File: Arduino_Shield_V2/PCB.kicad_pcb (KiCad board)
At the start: 2 copper layers, 68.6 x 53.3 mm, 18 parts, among them IC1 LTC6090HFE#PBF, J1 Power, J2 Digital/PWM, J3 Analog, J4 Digital/PWM, J6 Conn_01x01_Socket, U1 MCP4921

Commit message: Serious edits during 2/22 meeting by Eric
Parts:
- removed IC1: LTC6090HFE#PBF, LTC6090:SOP65P640X110-17N
- added C3: 0.1uF, Capacitor_SMD:C_1206_3216Metric_Pad1.33x1.80mm_HandSolder, F.Cu at (146.2, 81.5)
- added C4: 0.1uF, Capacitor_SMD:C_1206_3216Metric_Pad1.33x1.80mm_HandSolder, F.Cu at (131.5, 84.0)
- added J5: Conn_01x01, Connector_Pin:Pin_D1.0mm_L10.0mm, F.Cu at (160.4, 79.2)
- added J7: Conn_01x01, Connector_Pin:Pin_D1.0mm_L10.0mm, F.Cu at (160.4, 83.2)
- added J8: Conn_01x01, Connector_Pin:Pin_D1.0mm_L10.0mm, F.Cu at (160.4, 87.3)
- added U2: LTC6090, Package_SO:SOIC-8-1EP_3.9x4.9mm_P1.27mm_EP2.29x3mm, F.Cu at (138.3, 83.8)
- R1, R2, R3, R4, R5: footprint Resistor_THT:R_Axial_DIN0309_L9.0mm_D3.2mm_P12.70mm_Horizontal -> Resistor_SMD:R_1206_3216Metric_Pad1.30x1.75mm_HandSolder
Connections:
- J2 pad 1: /SCL/A5 -> unconnected-(J2-Pin_1-Pad1)
- J2 pad 2: /SDA/A4 -> unconnected-(J2-Pin_2-Pad2)
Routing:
- net GND: track 144.5 -> 0.00 mm, vias 3 -> 0
- net /SCL/A5: track 70.2 -> 0.00 mm
- net /SDA/A4: track 65.0 -> 0.00 mm
- net Net-(C2-Pad1): track 62.9 -> 16.0 mm
- net Net-(C2-Pad2): track 35.7 -> 14.3 mm
- net /*6: track 17.5 -> 0.00 mm
- net +5V: track 15.5 -> 0.00 mm
- net /*5: track 13.9 -> 0.00 mm
- net Net-(J6-Pin_1): track 12.5 -> 0.00 mm
- net Net-(U1-Vref): track 6.04 -> 17.2 mm
- net Net-(IC1-~{OD}): track 10.4 -> 0.00 mm
- net /4: track 10.3 -> 0.00 mm
- net /7: track 10.2 -> 0.00 mm
- net Net-(U1-Vout): track 5.05 -> 0.00 mm
- net Net-(C1-Pad1): track 18.7 -> 14.1 mm
- added copper zone on F.Cu, net GND

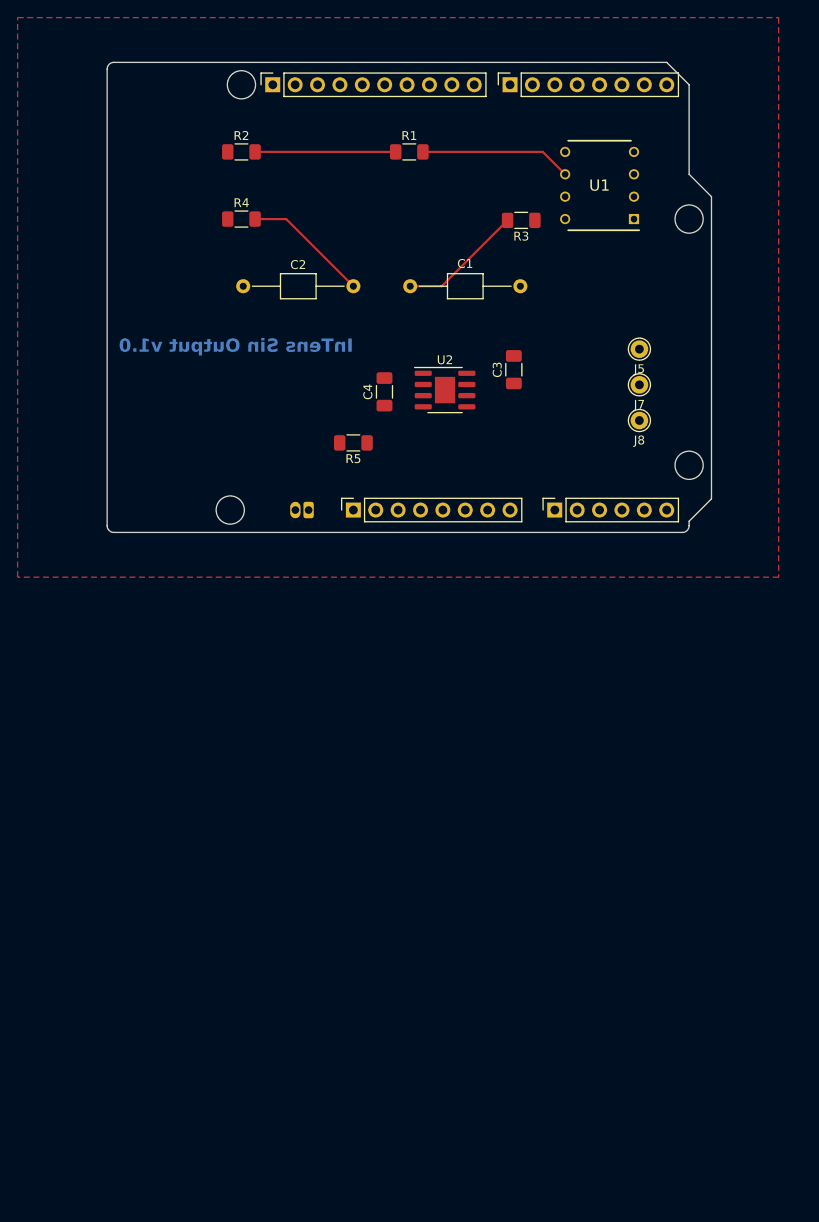
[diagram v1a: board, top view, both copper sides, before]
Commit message: fixed scematic wiring, PCB tracks, checked footprint dimensions, and added 3D models
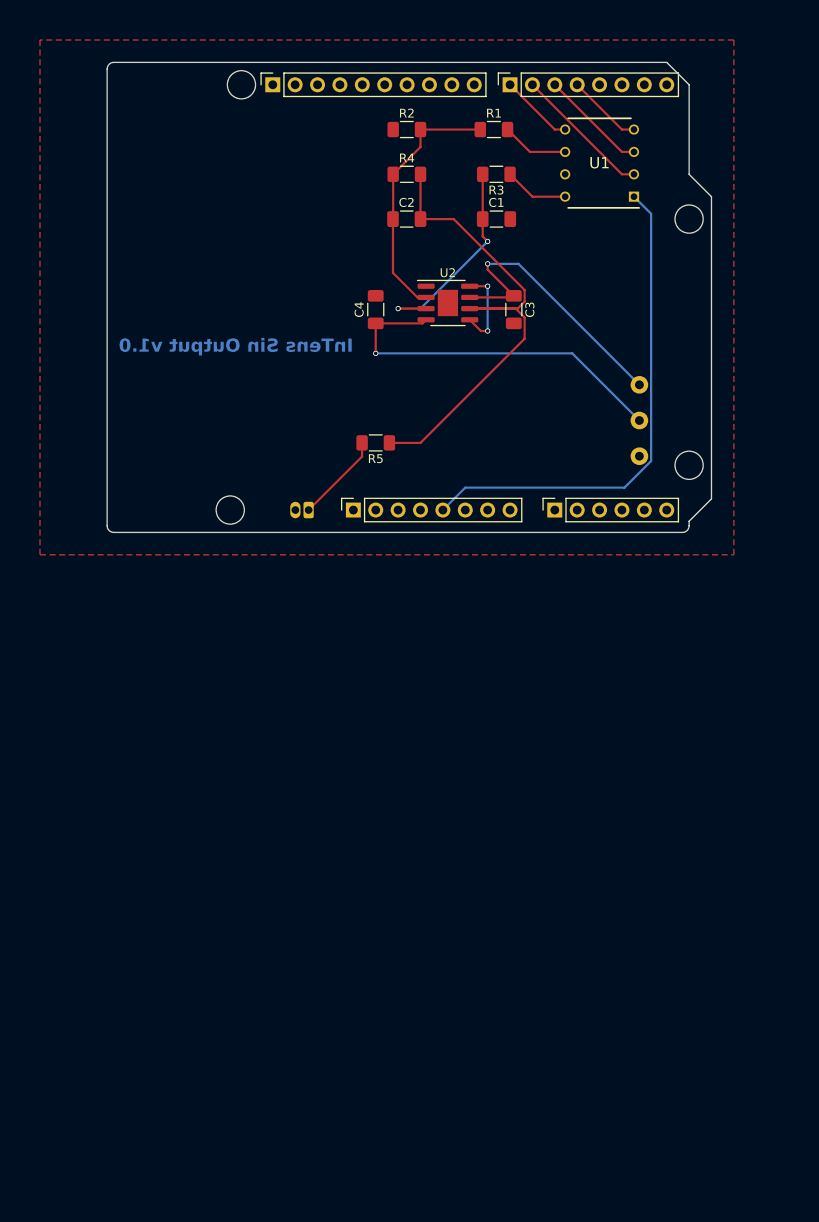
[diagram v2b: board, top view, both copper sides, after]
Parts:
- C1, C2: footprint Capacitor_THT:C_Axial_L3.8mm_D2.6mm_P12.50mm_Horizontal -> Capacitor_SMD:C_1206_3216Metric_Pad1.33x1.80mm_HandSolder
- J5, J7, J8: moved to B.Cu
- moved C2 20.1 mm to (134.0, 64.4)
- moved R4 19.4 mm to (134.0, 59.4)
- moved R2 18.9 mm to (134.0, 54.3)
- moved C1 12.4 mm to (144.2, 64.4)
- moved R1 9.93 mm to (143.9, 54.3)
- moved U2 9.89 mm to (138.7, 74.0)
- moved C4 9.39 mm to (130.5, 74.7)
- moved C3 6.82 mm to (146.2, 74.7), turned to -90 degrees
- moved R3 5.94 mm to (144.2, 59.4)
- moved J5 4.05 mm to (160.4, 83.2), turned to 180 degrees
- moved J7 4.05 mm to (160.4, 87.3), turned to 180 degrees
- moved J8 4.05 mm to (160.4, 91.3), turned to 180 degrees
- moved U1 2.54 mm to (155.9, 58.1)
- moved R5 2.54 mm to (130.5, 89.8)
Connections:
- U2 pad 1: unconnected-(U2-Pad1) -> GND
- U2 pad 5: unconnected-(U2-Pad5) -> Net-(U2-Pad5)
- U2 pad 8: unconnected-(U2-Pad8) -> Net-(U2-Pad5)
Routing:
- net +5V: track 0.00 -> 56.7 mm
- net Net-(C2-Pad2): track 14.3 -> 57.4 mm
- net -VSW: track 0.00 -> 42.4 mm, vias 0 -> 1
- net HT: track 0.00 -> 32.9 mm, vias 0 -> 1
- net /*6: track 0.00 -> 15.7 mm
- net Net-(C2-Pad1): track 16.0 -> 29.3 mm
- net /*5: track 0.00 -> 12.1 mm
- net Net-(C1-Pad1): track 14.1 -> 24.3 mm, vias 0 -> 2
- net Net-(J6-Pin_1): track 0.00 -> 10.1 mm
- net Net-(U2-Pad5): track 0.00 -> 9.68 mm, vias 0 -> 2
- net Net-(U1-Vref): track 17.2 -> 7.59 mm
- net /4: track 0.00 -> 8.55 mm
- net /7: track 0.00 -> 8.36 mm
- net Net-(U1-Vout): track 0.00 -> 7.31 mm

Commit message: Updated PCB (correct orientation)
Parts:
- C1, C2, C3, C4, R1, R2, R3, R4, R5, U1, U2: moved to B.Cu
- J5, J6, J7, J8: moved to F.Cu
- moved C4 15.2 mm to (145.7, 74.6), turned to -90 degrees
- moved C3 11.7 mm to (137.1, 82.2), turned to 0 degrees
- moved U1 5.08 mm to (150.8, 58.1), turned to -90 degrees
- moved C1 4.00 mm to (140.2, 64.4)
- moved R3 3.99 mm to (140.2, 59.4)
- moved R1 3.71 mm to (140.2, 54.3)
- moved R2 2.54 mm to (131.5, 54.3)
- moved R4 2.54 mm to (131.5, 59.4), turned to 180 degrees
- moved C2 2.52 mm to (131.5, 64.4), turned to 180 degrees
- moved U2 1.21 mm to (137.5, 74.0), turned to -90 degrees
- turned J5 to 0 degrees
- turned J6 to 0 degrees
- turned J7 to 0 degrees
- turned J8 to 0 degrees
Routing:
- net -VSW: track 42.4 -> 27.6 mm, vias 1 -> 0
- net Net-(C2-Pad2): track 57.4 -> 44.8 mm
- net Net-(C1-Pad1): track 24.3 -> 12.4 mm, vias 2 -> 0
- net /*6: track 15.7 -> 5.51 mm
- net /7: track 8.36 -> 16.5 mm
- net /*5: track 12.1 -> 5.51 mm
- net Net-(U1-Vref): track 7.59 -> 13.5 mm
- net Net-(U2-Pad5): track 9.68 -> 15.2 mm
- net +5V: track 56.7 -> 51.8 mm
- net Net-(C2-Pad1): track 29.3 -> 24.5 mm
- net /4: track 8.55 -> 5.51 mm
- net HT: track 32.9 -> 31.5 mm, vias 1 -> 0
- net Net-(U1-Vout): track 7.31 -> 6.35 mm
- added copper zone on B.Cu, net GND
- removed copper zone on F.Cu, net GND

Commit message: semi-updated from Eric 3/4 notes
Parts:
- added C5: 0.1 uF, Capacitor_SMD:C_1206_3216Metric_Pad1.33x1.80mm_HandSolder, B.Cu at (139.1, 89.8)
- moved J6 8.03 mm to (120.3, 89.8), turned to 180 degrees
- moved C4 5.08 mm to (150.8, 74.6)
- moved C3 3.21 mm to (139.1, 84.8)
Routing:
- net GND: track 0.00 -> 22.3 mm, vias 0 -> 1
- net +5V: track 51.8 -> 71.3 mm
- net -VSW: track 27.6 -> 39.2 mm, vias 0 -> 4
- net (no net): track 0.00 -> 3.82 mm, vias 0 -> 1
- net Net-(C2-Pad2): track 44.8 -> 48.4 mm, vias 0 -> 2
- net Net-(J6-Pin_1): track 10.1 -> 8.61 mm
- net HT: track 31.5 -> 32.1 mm
- net Net-(C2-Pad1): vias 0 -> 2
- net Net-(C1-Pad1): vias 0 -> 2

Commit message: updated PCB from 3/4 Eric Meeting
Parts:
- C1, C2, C3, C4, C5, R1, R2, R3, R4, R5, U1, U2: moved to F.Cu
- moved J6 30.9 mm to (150.8, 84.8), turned to -90 degrees
- moved C5 23.4 mm to (154.3, 72.1), turned to 180 degrees
- moved C4 18.3 mm to (132.6, 76.4), turned to 90 degrees
- moved R5 13.5 mm to (143.2, 85.2), turned to -90 degrees
- moved C3 12.1 mm to (147.8, 76.4), turned to -90 degrees
- moved U1 5.21 mm to (152.0, 63.2), turned to 180 degrees
- moved U2 3.52 mm to (140.1, 76.4), turned to 0 degrees
- moved C1 3.28 mm to (138.1, 67.0)
- moved R1 3.28 mm to (138.1, 56.8)
- moved R3 3.28 mm to (138.1, 61.9)
- moved C2 2.90 mm to (130.1, 67.0)
- moved R2 2.90 mm to (130.1, 56.8)
- moved R4 2.90 mm to (130.1, 61.9)
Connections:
- J6 pad 2: (no net) -> GND
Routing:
- net GND: track 22.3 -> 0.00 mm, vias 1 -> 0
- net Net-(C1-Pad1): track 12.4 -> 32.2 mm
- net +5V: track 71.3 -> 53.3 mm
- net /*6: track 5.51 -> 18.4 mm
- net HT: track 32.1 -> 21.7 mm
- net /*5: track 5.51 -> 14.8 mm
- net Net-(C2-Pad2): track 48.4 -> 39.6 mm, vias 2 -> 3
- net -VSW: track 39.2 -> 31.7 mm, vias 4 -> 0
- net /4: track 5.51 -> 11.2 mm
- net /7: track 16.5 -> 11.1 mm
- net Net-(U1-Vout): track 6.35 -> 10.5 mm
- net (no net): track 3.82 -> 0.00 mm, vias 1 -> 0
- net Net-(U1-Vref): track 13.5 -> 10.5 mm
- net Net-(U2-Pad5): track 15.2 -> 12.6 mm
- net Net-(C2-Pad1): track 24.5 -> 26.9 mm, vias 2 -> 0
- added copper zone on F.Cu, net GND
- removed copper zone on B.Cu, net GND

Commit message: ERIC: generate V1 gerbers with GND fixed
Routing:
- net GND: track 0.00 -> 6.98 mm, vias 0 -> 6
- added copper zone on B.Cu, net GND
- removed copper zone on F.Cu, net GND
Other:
- board text added: "+70V"
- board text added: "-70V"
- board text added: "GND"
- board text added: "OUT"
